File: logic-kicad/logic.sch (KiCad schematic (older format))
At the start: 24 parts

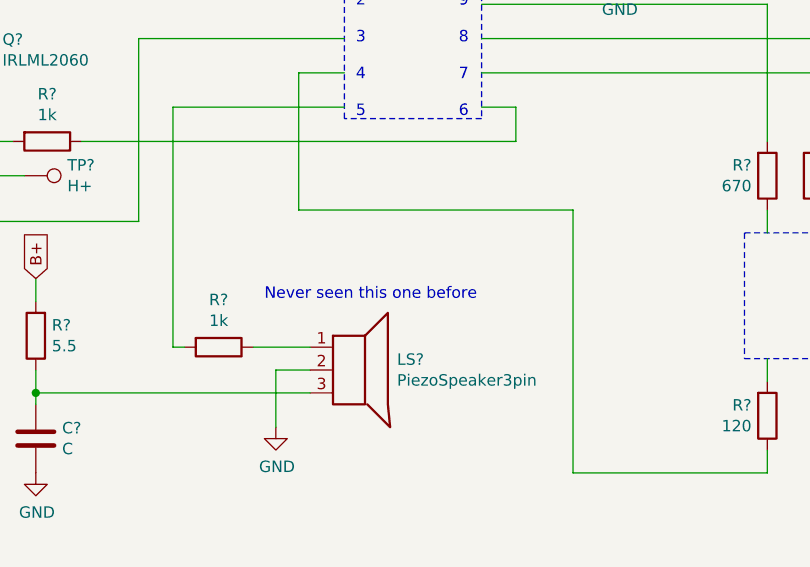
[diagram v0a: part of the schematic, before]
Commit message: comments and misnamed pictures
two pictures had their names swapped
added piezo mic dimensions
added footprints to the comments
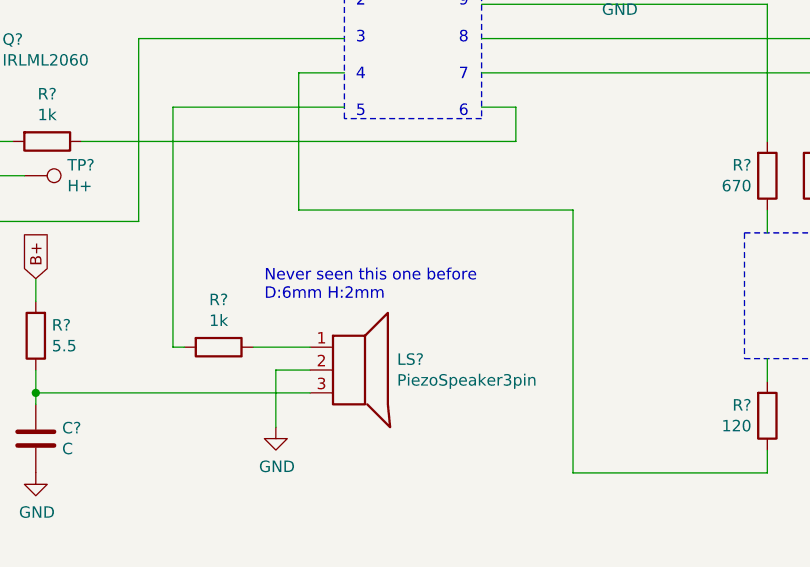
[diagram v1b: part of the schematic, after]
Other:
- note added: "Never seen this one before\nD:6mm H:2mm"
- note removed: "Never seen this one before"
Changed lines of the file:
@@
 PROBABLY N-Mosfet (no diode drops)\nD05JM\nSOT-23\npinout fits
 Text Notes 7000 4250 0    50   ~ 0
-Never seen this one before
+Never seen this one before\nD:6mm H:2mm
 $Comp
 L Device:C C?

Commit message: LEDs investigated
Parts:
- added D?: ORG, symbol Device:LED
- added D?: WHT, symbol Device:LED
- added D?: RED, symbol Device:LED
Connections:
- wire segments 83 -> 90
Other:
- note added: "Green mark side"
- note added: "Never seen this one before\n3 terminal mic: G/-/+\nD:6mm H:2mm"
- note added: "Three LEDs in 4-pin package\nValid pin-wise"
- note removed: "Never seen this one before\nD:6mm H:2mm"
- note removed: "Weird (?) dual LEDs\nNeed to investigate further"
- moved on the sheet: R?
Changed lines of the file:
@@
 10\n\n9\n\n8\n\n7\n\n6
 Wire Wire Line
-	7350 2750 7200 2750
-Text GLabel 7200 2750 0    50   Input ~ 0
+	7350 2800 7200 2800
+Text GLabel 7200 2800 0    50   Input ~ 0
 B+
 $Comp
 L power:GND #PWR?
 U 1 1 6129630A
-P 8550 2800
-F 0 "#PWR?" H 8550 2550 50  0001 C CNN
-F 1 "GND" H 8555 2627 50  0000 C CNN
-F 2 "" H 8550 2800 50  0001 C CNN
-F 3 "" H 8550 2800 50  0001 C CNN
-	1    8550 2800
-	1    0    0    -1
-$EndComp
-Wire Wire Line
-	7950 2750 8550 2750
-Wire Wire Line
-	8550 2750 8550 2800
+P 9200 2850
+F 0 "#PWR?" H 9200 2600 50  0001 C CNN
+F 1 "GND" H 9205 2677 50  0000 C CNN
+F 2 "" H 9200 2850 50  0001 C CNN
+F 3 "" H 9200 2850 50  0001 C CNN
+	1    9200 2850
+	1    0    0    -1
+$EndComp
 Wire Wire Line
 	5750 3350 5750 3550
@@
 Wire Wire Line
 	5200 2650 6650 2650
-Wire Wire Line
-	6650 2650 6650 2900
-Wire Wire Line
-	6650 2900 7350 2900
 $Comp
 L Moje:PiezoSpeaker3pin LS?
@@
 	1    0    0    -1
 $EndComp
-Wire Notes Line
-	9100 3950 9500 3950
-Wire Notes Line
-	9500 3950 9500 4500
-Wire Notes Line
-	9100 3950 9100 4500
-Wire Notes Line
-	9100 4500 9500 4500
 $Comp
 L Device:R R?
 U 1 1 612A5DDB
-P 9200 3700
-F 0 "R?" H 9131 3654 50  0000 R CNN
-F 1 "670" H 9131 3745 50  0000 R CNN
-F 2 "" V 9130 3700 50  0001 C CNN
-F 3 "~" H 9200 3700 50  0001 C CNN
-	1    9200 3700
+P 9100 3700
+F 0 "R?" H 9031 3654 50  0000 R CNN
+F 1 "670" H 9031 3745 50  0000 R CNN
+F 2 "" V 9030 3700 50  0001 C CNN
+F 3 "~" H 9100 3700 50  0001 C CNN
+	1    9100 3700
 	1    0    0    1
 $EndComp
@@
 L Device:R R?
 U 1 1 612A68BF
-P 9200 4750
-F 0 "R?" H 9131 4704 50  0000 R CNN
-F 1 "120" H 9131 4795 50  0000 R CNN
-F 2 "" V 9130 4750 50  0001 C CNN
-F 3 "~" H 9200 4750 50  0001 C CNN
-	1    9200 4750
+P 8750 4800
+F 0 "R?" H 8681 4754 50  0000 R CNN
+F 1 "120" H 8681 4845 50  0000 R CNN
+F 2 "" V 8680 4800 50  0001 C CNN
+F 3 "~" H 8750 4800 50  0001 C CNN
+	1    8750 4800
 	1    0    0    1
 $EndComp
-Text GLabel 9600 4700 2    50   Input ~ 0
-B+
-Wire Wire Line
-	9600 4700 9400 4700
-Wire Wire Line
-	9400 4700 9400 4500
-Wire Wire Line
-	9200 4600 9200 4500
-Wire Wire Line
-	9200 3850 9200 3950
-Wire Wire Line
-	9400 3850 9400 3950
-Wire Wire Line
-	9200 4900 9200 5000
-Wire Wire Line
-	9200 5000 8350 5000
-Wire Wire Line
-	8350 5000 8350 3850
+Text GLabel 9400 4700 2    50   Input ~ 0
+B+
+Wire Wire Line
+	8750 4950 8750 5050
 Wire Wire Line
 	8350 3850 7150 3850
@@
 Wire Wire Line
 	7150 3250 7350 3250
-Wire Wire Line
-	7950 2950 9200 2950
-Wire Wire Line
-	9200 2950 9200 3550
-Wire Wire Line
-	9400 3550 9400 3100
-Wire Wire Line
-	9400 3100 7950 3100
 $Comp
 L Device:R R?
@@
 Text Notes 7350 2650 0    50   ~ 0
 19A2\nSome custom logic\nTSSOP-10 (?)
-Text Notes 9500 4300 0    50   ~ 0
-Weird (?) dual LEDs\nNeed to investigate further
+Text Notes 9600 4050 0    50   ~ 0
+Three LEDs in 4-pin package\nValid pin-wise
 Text Notes 4300 4450 0    50   ~ 0
 Probably simplest battery charging IC\nB19G\nSOT-23-5\nMCP73831 maybe?
@@
 PROBABLY N-Mosfet (no diode drops)\nD05JM\nSOT-23\npinout fits
 Text Notes 7000 4250 0    50   ~ 0
-Never seen this one before\nD:6mm H:2mm
+Never seen this one before\n3 terminal mic: G/-/+\nD:6mm H:2mm
 $Comp
 L Device:C C?
@@
 	1    0    0    -1
 $EndComp
+$Comp
+L Device:LED D?
+U 1 1 612E3F2E
+P 9400 4250
+F 0 "D?" V 9347 4330 50  0000 L CNN
+F 1 "ORG" V 9438 4330 50  0000 L CNN
+F 2 "" H 9400 4250 50  0001 C CNN
+F 3 "~" H 9400 4250 50  0001 C CNN
+	1    9400 4250
+	0    1    1    0
+$EndComp
+$Comp
+L Device:LED D?
+U 1 1 612E9797
+P 9100 4250
+F 0 "D?" V 9047 4330 50  0000 L CNN
+F 1 "WHT" V 9138 4330 50  0000 L CNN
+F 2 "" H 9100 4250 50  0001 C CNN
+F 3 "~" H 9100 4250 50  0001 C CNN
+	1    9100 4250
+	0    1    1    0
+$EndComp
+$Comp
+L Device:LED D?
+U 1 1 612E9A5E
+P 8800 4250
+F 0 "D?" V 8747 4330 50  0000 L CNN
+F 1 "RED" V 8838 4330 50  0000 L CNN
+F 2 "" H 8800 4250 50  0001 C CNN
+F 3 "~" H 8800 4250 50  0001 C CNN
+	1    8800 4250
+	0    1    1    0
+$EndComp
+Wire Wire Line
+	9100 3850 9100 4100
+Wire Wire Line
+	9400 3850 9400 4100
+Wire Wire Line
+	8800 4100 8800 4050
+Wire Wire Line
+	9100 4700 9100 4450
+Wire Wire Line
+	9100 4450 8800 4450
+Wire Wire Line
+	8800 4450 8800 4400
+Wire Wire Line
+	9100 4700 9400 4700
+Wire Wire Line
+	9100 4400 9100 4450
+Connection ~ 9100 4450
+Wire Wire Line
+	9100 4450 9400 4450
+Wire Wire Line
+	9400 4450 9400 4400
+Wire Notes Line
+	8700 3900 9500 3900
+Wire Notes Line
+	9500 3900 9500 4500
+Wire Notes Line
+	9500 4500 8700 4500
+Wire Notes Line
+	8700 4500 8700 3900
+Wire Wire Line
+	7950 2950 9100 2950
+Wire Wire Line
+	9400 3100 7950 3100
+Wire Wire Line
+	9400 3100 9400 3550
+Wire Wire Line
+	9100 3550 9100 2950
+Text Notes 8800 4600 0    50   ~ 0
+Green mark side
+Wire Wire Line
+	8800 4050 8750 4050
+Wire Wire Line
+	8750 4050 8750 4650
+Wire Wire Line
+	8350 3850 8350 5050
+Wire Wire Line
+	8350 5050 8750 5050
+Wire Wire Line
+	7350 2950 6650 2950
+Wire Wire Line
+	6650 2650 6650 2950
+Wire Wire Line
+	7950 2800 9200 2800
+Wire Wire Line
+	9200 2800 9200 2850
 $EndSCHEMATC
